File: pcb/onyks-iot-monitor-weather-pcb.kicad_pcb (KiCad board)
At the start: 2 copper layers, 100 x 82 mm, 32 parts, among them J1 53398-0371, J10 Conn_01x02_Pin, J11 Conn_01x06_Pin, J12 Conn_02x05_Odd_Even, J13 Conn_01x02_Pin, J2 53398-0371, J3 53048-0810, J4 53398-0371, J5 53398-0371, J6 53398-0371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

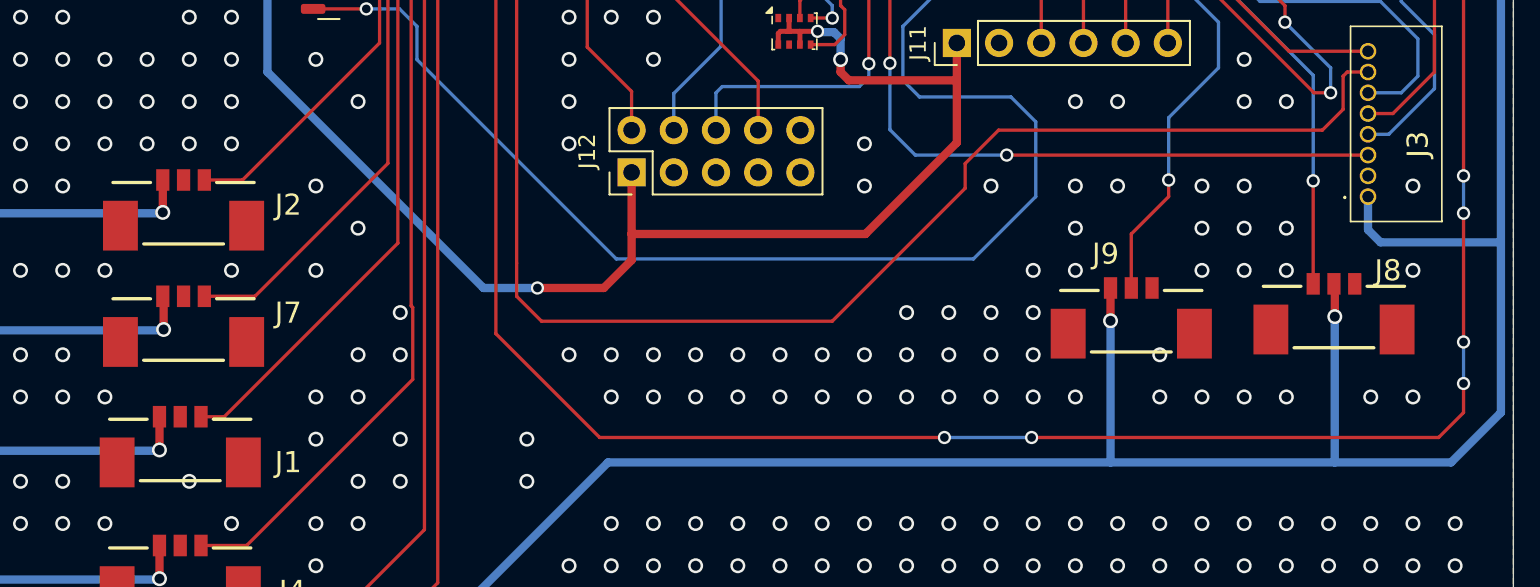
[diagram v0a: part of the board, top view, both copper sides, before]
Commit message: Aded Readme, change schematic layout, added block diagrams
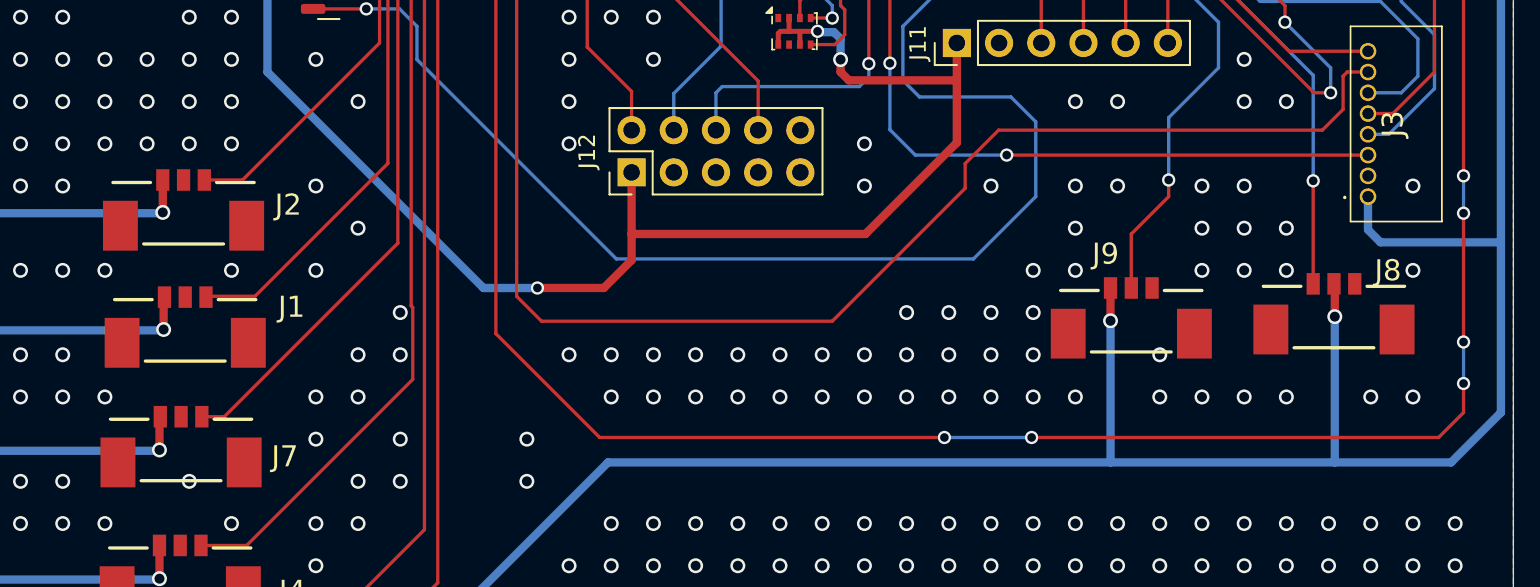
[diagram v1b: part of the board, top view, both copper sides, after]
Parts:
- moved J7 7.25 mm to (112.5, 88.2)
- moved J1 7.21 mm to (112.8, 81.0)
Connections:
- J1 pad 3: /Hall 6 -> /Hall 4
- J7 pad 3: /Hall 4 -> /Hall 6

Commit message: Poprawki w schemacie elektrycznym
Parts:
- C1, C6, C7, C8: value 22uF -> 22uF/4VDC
- C2, C3, C4, C5: value 0.1uF -> 0.1uF/4VDC
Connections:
- net /3V3 renamed +3.3V
- U3 pad 3: /EN -> VCC
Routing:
- net /EN: track 200.1 -> 174.0 mm, vias 12 -> 10
- net VCC: track 362.9 -> 366.5 mm

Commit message: Dalsze zmiany w schemacie elektrycznym - przewidywane duże zmiany w PCB
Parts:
- added J3: Conn_01x04_Pin, 1bmoje:533980471- MOLEXx4, F.Cu at (72.0, 83.5)
- added R10: 470, Resistor_SMD:R_0603_1608Metric, F.Cu at (71.0, 95.3)
- added R11: 910, Resistor_SMD:R_0603_1608Metric, F.Cu at (71.0, 97.8)
- added R12: 470, Resistor_SMD:R_0603_1608Metric, F.Cu at (75.0, 90.3)
- added R13: 910, Resistor_SMD:R_0603_1608Metric, F.Cu at (75.0, 92.8)
- added R14: 470, Resistor_SMD:R_0603_1608Metric, F.Cu at (75.0, 95.3)
- added R15: 910, Resistor_SMD:R_0603_1608Metric, F.Cu at (75.0, 97.8)
- added R4: 470, Resistor_SMD:R_0603_1608Metric, F.Cu at (67.0, 90.3)
- added R5: 910, Resistor_SMD:R_0603_1608Metric, F.Cu at (67.0, 92.8)
- added R6: 470, Resistor_SMD:R_0603_1608Metric, F.Cu at (67.0, 95.3)
- added R7: 910, Resistor_SMD:R_0603_1608Metric, F.Cu at (67.0, 97.8)
- added R8: 470, Resistor_SMD:R_0603_1608Metric, F.Cu at (71.0, 90.3)
- added R9: 910, Resistor_SMD:R_0603_1608Metric, F.Cu at (71.0, 92.8)
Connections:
- J1 pad 3: /Hall 4 -> Net-(J1-Pin_3)
- J2 pad 3: /Hall 5 -> Net-(J2-Pin_3)
- J4 pad 3: /Hall 1 -> Net-(J4-Pin_3)
- J5 pad 3: /Hall 2 -> Net-(J5-Pin_3)
- J6 pad 3: /Hall 3 -> Net-(J6-Pin_3)
- J7 pad 3: /Hall 6 -> Net-(J7-Pin_3)
- Q1 pad 2: Net-(J10-Pin_2) -> /UART_PROGRAM_RTS
- Q2 pad 2: /IO0 -> /UART_PROGRAM_DTR
- Q2 pad 3: Net-(J10-Pin_1) -> /IO0
- R2 pad 1: Net-(J10-Pin_1) -> /UART_PROGRAM_DTR
- R3 pad 1: Net-(J10-Pin_2) -> /UART_PROGRAM_RTS
- U1 pad 24: /PMS_SET -> unconnected-(U1-IO2-Pad24)
- U1 pad 30: /UART_PROGRAM_DTR -> unconnected-(U1-IO18-Pad30)
- U1 pad 31: /UART_PROGRAM_RTS -> unconnected-(U1-IO19-Pad31)
- U1 pad 33: /PMS_SELECT -> unconnected-(U1-IO21-Pad33)
- U1 pad 34: /PMS_RXD -> unconnected-(U1-RXD0/IO3-Pad34)
- U1 pad 35: /PMS_TXD -> unconnected-(U1-TXD0/IO1-Pad35)
- U1 pad 36: /PMS_RESET -> /MQ135_DOUT
- U1 pad 7: /PMS_PWM -> /MQ135_AOUT
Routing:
- net Net-(J10-Pin_1): vias 2 -> 0
- net /UART_PROGRAM_DTR: vias 0 -> 2

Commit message: zrobiony PCB
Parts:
- removed C1, C7, C8: 22uF/4VDC, Capacitor_SMD:C_0603_1608Metric
- removed C2: 0.1uF/4VDC, Capacitor_SMD:C_0603_1608Metric
- removed J11: Conn_01x06_Pin, Connector_PinHeader_2.54mm:PinHeader_1x06_P2.54mm_Vertical
- removed J12: Conn_02x05_Odd_Even, Connector_PinHeader_2.54mm:PinHeader_2x05_P2.54mm_Vertical
- removed the J3 at (184.0, 74.8)
- removed the J3 at (72.0, 83.5)
- removed Q1, Q2: SS8050, Package_TO_SOT_SMD:SOT-23
- removed R2, R3: 10K, Resistor_SMD:R_0603_1608Metric
- removed U3: TLV75733PDBV, Package_TO_SOT_SMD:SOT-23-5
- removed U6: BMP280, Package_LGA:Bosch_LGA-8_2x2.5mm_P0.65mm_ClockwisePinNumbering
- added C11: 22uF/10VDC, Capacitor_SMD:C_0603_1608Metric, F.Cu at (97.0, 40.2)
- added C12: 0.1uF/10VDC, Capacitor_SMD:C_0603_1608Metric, F.Cu at (99.2, 46.2)
- added C13: 0.1uF/10VDC, Capacitor_SMD:C_0603_1608Metric, F.Cu at (100.2, 40.2)
- added J14: Conn_02x05_Odd_Even, Connector_PinHeader_2.54mm:PinHeader_2x05_P2.54mm_Vertical, F.Cu at (105.4, 76.1)
- added J3: Conn_01x04_Pin, 1bmoje:533980471- MOLEXx4, F.Cu at (137.8, 89.8)
- added Q3: SS8050, Package_TO_SOT_SMD:SOT-23, F.Cu at (93.9, 46.2)
- added Q4: SS8050, Package_TO_SOT_SMD:SOT-23, F.Cu at (131.1, 56.0)
- added R16: 10K, Resistor_SMD:R_0603_1608Metric, F.Cu at (132.0, 60.0)
- added R17: 10K, Resistor_SMD:R_0603_1608Metric, F.Cu at (86.6, 44.2)
- added U2: BMP280, Package_LGA:Bosch_LGA-8_2x2.5mm_P0.65mm_ClockwisePinNumbering, F.Cu at (113.4, 65.0)
- added U5: ESP32-WROOM-32D, RF_Module:ESP32-WROOM-32D, F.Cu at (114.0, 47.7)
- C3, C4: value 0.1uF/4VDC -> 22uF/10VDC
- C6: value 22uF/4VDC -> 0.1uF/4VDC
- J10: value Conn_01x02_Pin -> Conn_01x06_Pin; footprint Connector_PinHeader_2.54mm:PinHeader_1x02_P2.54mm_Vertical -> Connector_PinHeader_2.54mm:PinHeader_1x06_P2.54mm_Vertical
- R11, R13: value 910 -> 470
- R6, R8: value 470 -> 910
- U1: value ESP32-WROOM-32D -> TLV75733PDBV; footprint RF_Module:ESP32-WROOM-32D -> Package_TO_SOT_SMD:SOT-23-5
- moved C4 107.8 mm to (76.0, 45.6), turned to 90 degrees
- moved U1 76.6 mm to (72.9, 48.5)
- moved C3 59.5 mm to (69.8, 45.6)
- moved C5 51.8 mm to (132.0, 46.6), turned to -90 degrees
- moved J10 50.3 mm to (99.2, 105.8), turned to -90 degrees
- moved R1 46.0 mm to (87.2, 47.0), turned to 0 degrees
- moved S1 43.3 mm to (139.9, 48.2), turned to 180 degrees
- moved S2 43.1 mm to (140.0, 54.0), turned to 180 degrees
- moved J8 42.9 mm to (139.6, 73.2), turned to 180 degrees
- moved J13 40.7 mm to (62.0, 48.0)
- moved C6 39.5 mm to (147.4, 54.0), turned to 0 degrees
- moved J6 39.2 mm to (77.4, 92.8)
- moved J5 38.6 mm to (77.4, 86.9)
- moved J4 38.1 mm to (77.4, 81.0)
- moved J1 37.8 mm to (77.4, 67.6)
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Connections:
- C3 pad 1: /EN -> VCC
- C4 pad 1: GND -> +3.3V
- C4 pad 2: /IO0 -> GND
- C5 pad 2: /EN -> /ESP32/IO0
- C6 pad 1: VCC -> GND
- C6 pad 2: GND -> /ESP32/EN
- D1 pad 4: /LED -> /ESP32/LED
- J10 pad 1: Net-(J10-Pin_1) -> +3.3V
- J10 pad 2: Net-(J10-Pin_2) -> GND
- J8 pad 1: /SEN0219 -> VCC
- J8 pad 2: VCC -> /ESP32/IO4
- J9 pad 1: VCC -> /ESP32/IO5
- J9 pad 2: /DHT22 -> VCC
- R1 pad 1: +3.3V -> /ESP32/UART_PROGRAM_DTR
- R1 pad 2: /EN -> Net-(Q3-B)
- R10 pad 1: Net-(J5-Pin_3) -> Net-(J6-Pin_3)
- R10 pad 2: /Hall 2 -> /ESP32/IO27
- R11 pad 1: /Hall 2 -> Net-(J4-Pin_3)
- R11 pad 2: GND -> /ESP32/IO25
- R12 pad 1: Net-(J6-Pin_3) -> Net-(J5-Pin_3)
- R12 pad 2: /Hall 3 -> /ESP32/IO26
- R13 pad 1: /Hall 3 -> Net-(J7-Pin_3)
- R13 pad 2: GND -> /ESP32/IO33
- R14 pad 1: Net-(J7-Pin_3) -> Net-(J2-Pin_3)
- R14 pad 2: /Hall 6 -> /ESP32/IO34
- R15 pad 1: /Hall 6 -> /ESP32/IO34
- R4 pad 2: /Hall 4 -> /ESP32/IO32
- R5 pad 1: /Hall 4 -> /ESP32/IO27
- R6 pad 1: Net-(J2-Pin_3) -> /ESP32/IO25
- R6 pad 2: /Hall 5 -> GND
- R7 pad 1: /Hall 5 -> /ESP32/IO26
- R8 pad 1: Net-(J4-Pin_3) -> /ESP32/IO33
- R8 pad 2: /Hall 1 -> GND
- R9 pad 1: /Hall 1 -> /ESP32/IO32
- S1 pad 2: /IO0 -> /ESP32/IO0
- S2 pad 2: /EN -> /ESP32/EN
- U1 pad 1: GND -> VCC
- U1 pad 2: +3.3V -> GND
- U1 pad 3: /EN -> VCC
- U1 pad 5: unconnected-(U1-SENSOR_VN-Pad5) -> +3.3V
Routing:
- net +3.3V: track 138.0 -> 312.7 mm, vias 4 -> 6
- net /EN: track 174.0 -> 0.00 mm, vias 10 -> 0
- net /IO0: track 153.6 -> 0.00 mm, vias 7 -> 0
- net /ESP32/UART_PROGRAM_DTR: track 0.00 -> 140.7 mm, vias 0 -> 4
- net /ESP32/UART_PROGRAM_RTS: track 0.00 -> 138.5 mm, vias 0 -> 4
- net /ESP32/EN: track 0.00 -> 118.4 mm, vias 0 -> 3
- net /PMS_PWM: track 97.7 -> 0.00 mm, vias 2 -> 0
- net /ESP32/IO35: track 0.00 -> 83.1 mm, vias 0 -> 4
- net /ESP32/UART_PROGRAM_TXD: track 0.00 -> 82.0 mm, vias 0 -> 2
- net /ESP32/UART_PROGRAM_RXD: track 0.00 -> 77.0 mm, vias 0 -> 3
- net /Hall 3: track 74.1 -> 0.00 mm
- net /Hall 2: track 69.5 -> 0.00 mm
- net /Hall 1: track 62.0 -> 0.00 mm
- net /ESP32/IO22: track 0.00 -> 61.1 mm, vias 0 -> 2
- net VCC: track 366.5 -> 305.4 mm, vias 10 -> 2
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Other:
- board size 100 x 82 mm -> 100 x 100 mm
